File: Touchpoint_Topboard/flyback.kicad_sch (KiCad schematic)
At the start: 18 parts, among them Q1 NMOS, T1 DA2033-AL, U1 LT3750AEMS-TRPBF

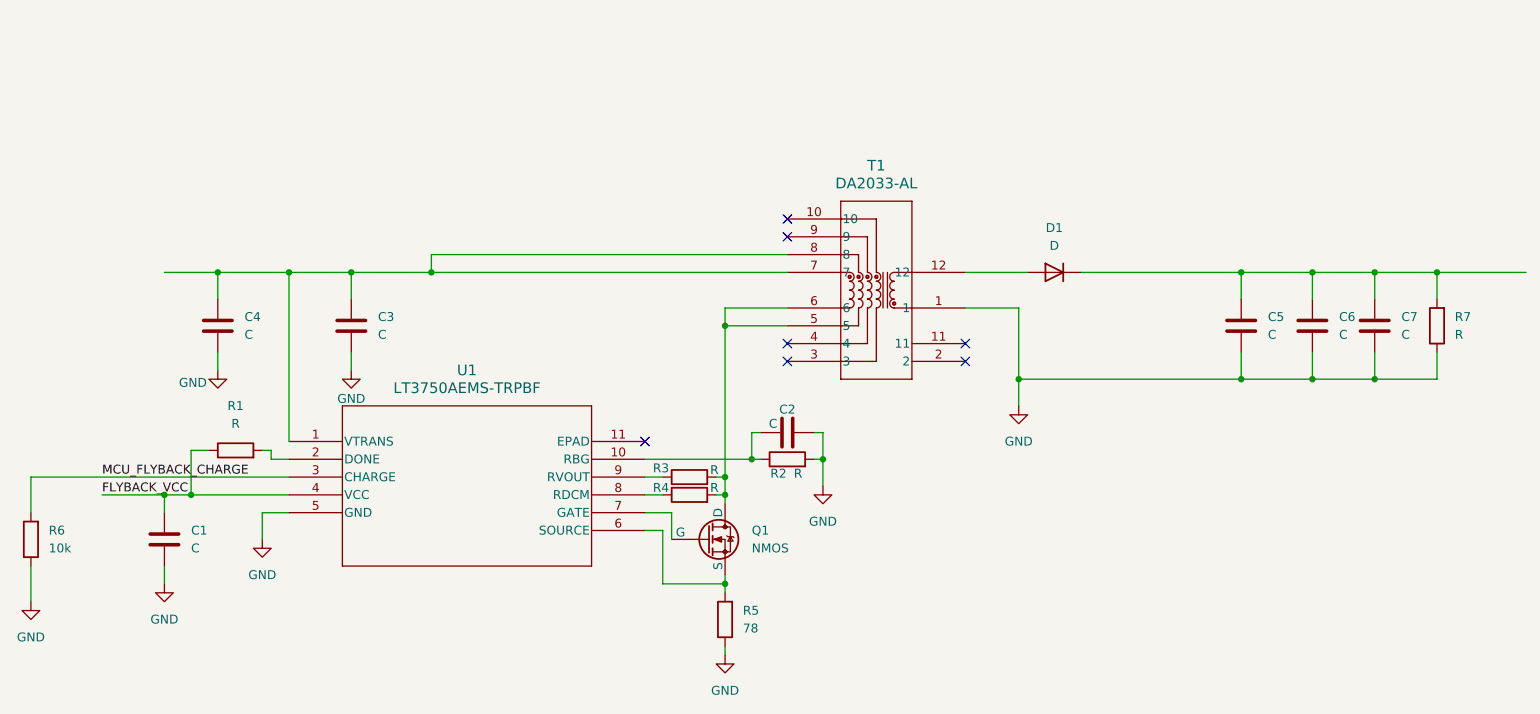
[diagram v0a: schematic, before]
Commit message: Finished assigning most footprints
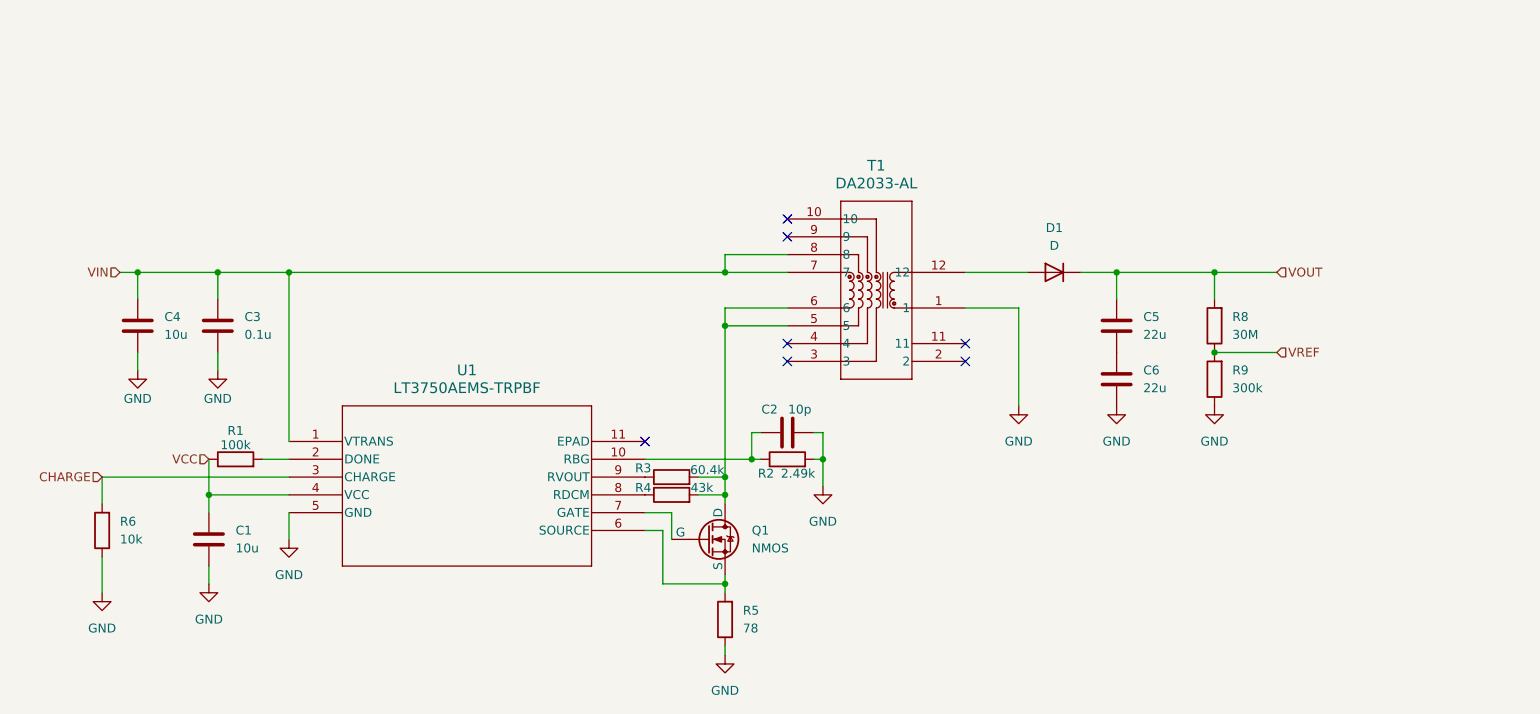
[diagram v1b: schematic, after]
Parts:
- removed C7: C, symbol Device:C
- removed R7: R, symbol Device:R
- added R8: 30M, Resistor_SMD:R_0402_1005Metric, symbol Device:R
- added R9: 300k, Resistor_SMD:R_0402_1005Metric, symbol Device:R
- C1, C4: value C -> 10u; footprint (none) -> Capacitor_SMD:C_0805_2012Metric
- C2: value C -> 10p; footprint (none) -> Capacitor_SMD:C_0402_1005Metric
- C3: value C -> 0.1u; footprint (none) -> Capacitor_SMD:C_0402_1005Metric
- C5, C6: value C -> 22u; footprint (none) -> Capacitor_SMD:C_0805_2012Metric
- D1: footprint (none) -> Touchpoint:SMB_DIO
- Q1: footprint (none) -> Touchpoint:SOT-89_3MC_MCH
- R1: value R -> 100k; footprint (none) -> Resistor_SMD:R_0402_1005Metric
- R2: value R -> 2.49k; footprint (none) -> Resistor_SMD:R_0402_1005Metric
- R3: value R -> 60.4k; footprint (none) -> Resistor_SMD:R_0402_1005Metric
- R4: value R -> 43k; footprint (none) -> Resistor_SMD:R_0402_1005Metric
- R5, R6: footprint (none) -> Resistor_SMD:R_0402_1005Metric
- T1: footprint DA2033-AL_COC -> Touchpoint:DA2032-AL
- U1: footprint MSOP10_05-08-1664_ADI -> Touchpoint:MSOP10_05-08-1664_ADI
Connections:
- net GND: now also C2.1, R9.1; no longer C2.2, C5.2
- net VOUT: now reaches C5.1, D1.1 (K)
- net VOUT: now also R8.2; no longer C6.1
- net VIN: now reaches C3.1, C4.1, T1.7, T1.8, U1.1 (VTRANS)
- net at R2.1, U1.10 (RBG): now also C2.2; no longer C2.1
- net FLYBACK_VCC renamed VCC
- net MCU_FLYBACK_CHARGE renamed CHARGE
- new net: C5.2, C6.1
- new net VREF: R8.1, R9.2
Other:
- moved on the sheet: C1, C3, C4, C5, R1, R3, R4, R6

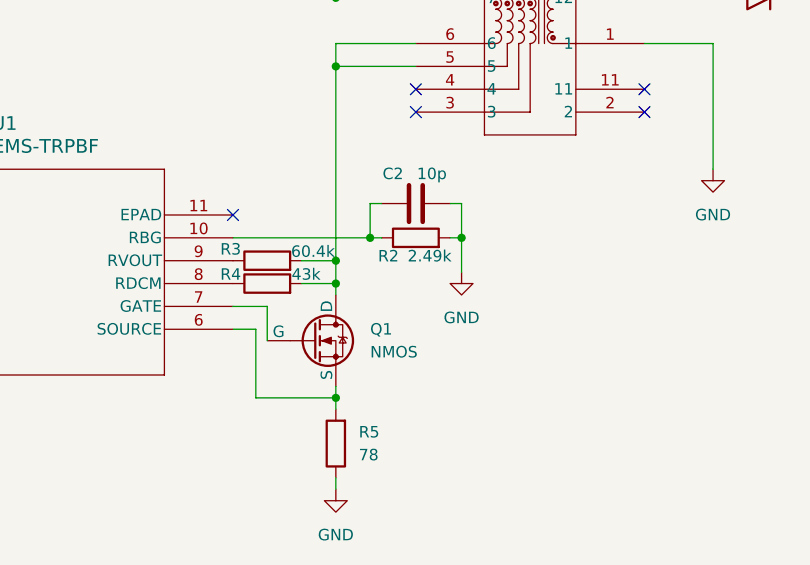
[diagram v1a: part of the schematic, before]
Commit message: Changed some component values based on availability
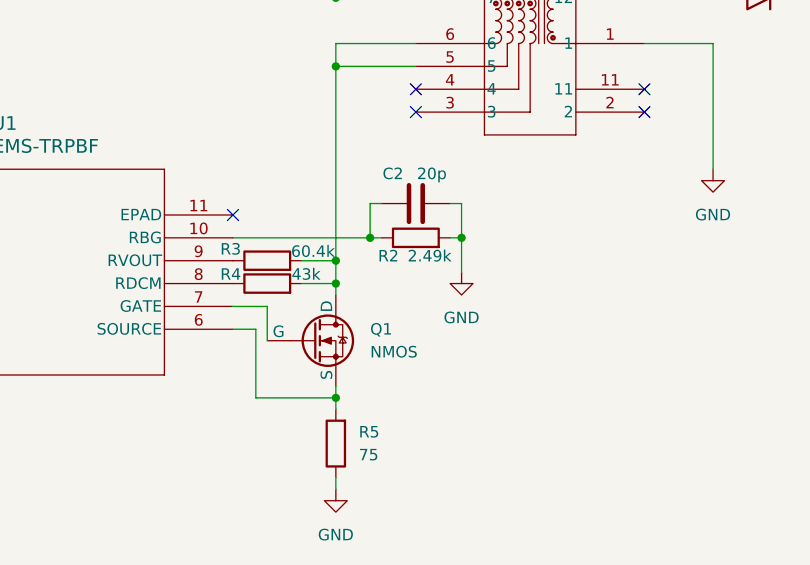
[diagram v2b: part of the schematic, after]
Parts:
- C2: value 10p -> 20p
- R5: value 78 -> 75
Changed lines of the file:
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@@
 			)
 		)
-		(property "Value" "78"
+		(property "Value" "75"
 			(at 171.45 118.1099 0)
 			(effects
@@
 			)
 		)
-		(property "Value" "10p"
+		(property "Value" "20p"
 			(at 179.578 86.868 90)
 			(effects

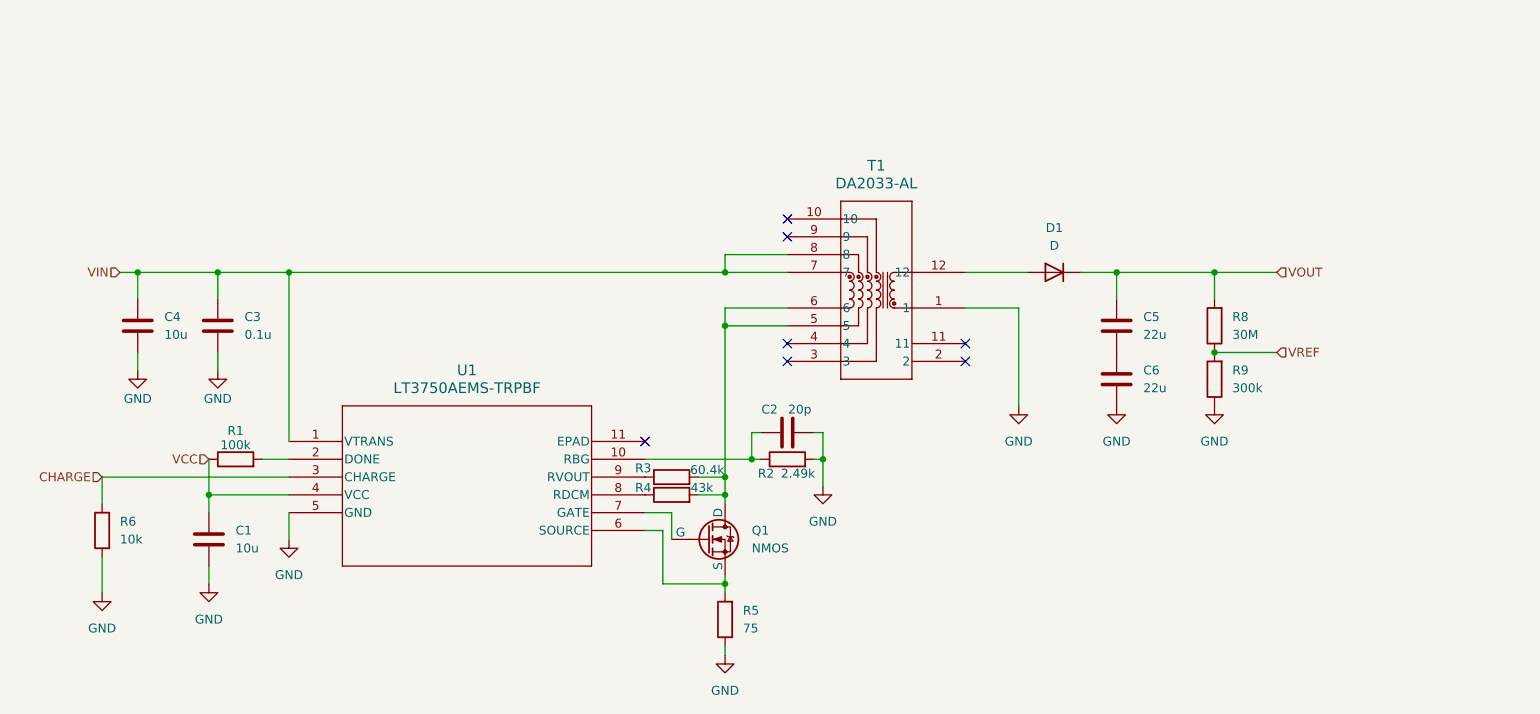
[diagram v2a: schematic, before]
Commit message: Finished assigning footprints and 3d models for both boards
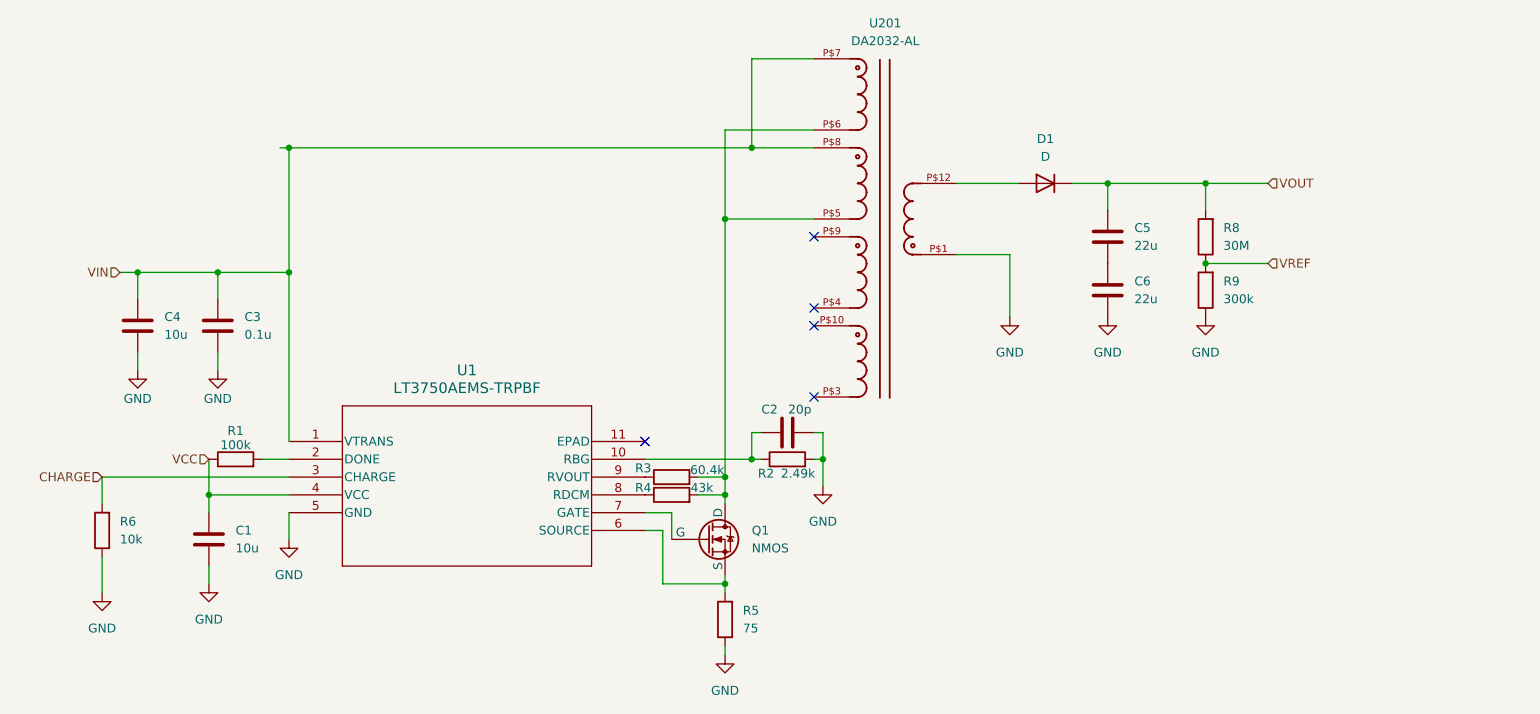
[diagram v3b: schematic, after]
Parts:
- removed T1: DA2033-AL, Touchpoint:DA2032-AL, symbol DL2032:DA2033-AL
- added U201: DA2032-AL, Touchpoint:DA2032-AL, symbol DA2032-AL:DA2032-AL
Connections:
- net GND: now also U201.P$1
- net VIN: now also U201.P$7, U201.P$8
- net at Q1.1 (D), R3.2, R4.2: now also U201.P$5, U201.P$6
- net at D1.2 (A): now also U201.P$12
- no-connect marks 7 -> 5
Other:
- moved on the sheet: C5, C6, D1, R8, R9

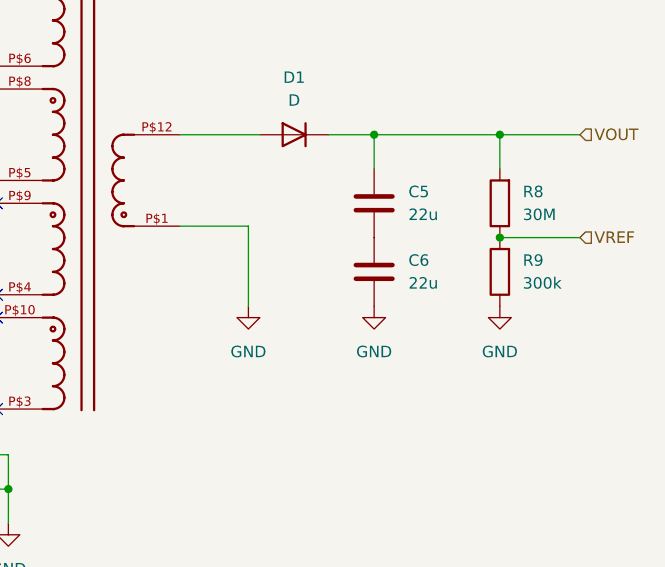
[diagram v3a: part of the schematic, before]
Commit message: Actually finished assigning footprints in 3d models
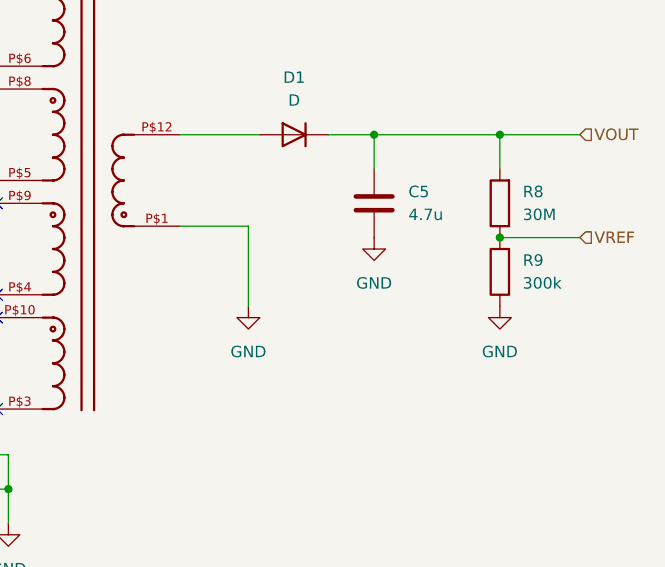
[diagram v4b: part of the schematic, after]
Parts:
- removed C6: 22u, Capacitor_SMD:C_0805_2012Metric, symbol Device:C
- C5: value 22u -> 4.7u; footprint Capacitor_SMD:C_0805_2012Metric -> Capacitor_THT:CP_Radial_D8.0mm_P3.50mm
- U1: footprint Touchpoint:MSOP10_05-08-1664_ADI -> Package_SO:MSOP-10-1EP_3x3mm_P0.5mm_EP1.68x1.88mm
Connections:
- net GND: now also C5.2
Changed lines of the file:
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@@
 	(symbol
 		(lib_id "power:GND")
-		(at 223.52 73.66 0)
+		(at 223.52 66.04 0)
 		(unit 1)
 		(exclude_from_sim no)
@@
 		(fields_autoplaced yes)
 		(property "Reference" "#PWR016"
-			(at 223.52 80.01 0)
+			(at 223.52 72.39 0)
 			(effects
 				(font
@@
 		)
 		(property "Value" "GND"
-			(at 223.52 78.74 0)
+			(at 223.52 71.12 0)
 			(effects
 				(font
@@
 		)
 		(property "Footprint" ""
-			(at 223.52 73.66 0)
+			(at 223.52 66.04 0)
 			(effects
 				(font
@@
 		)
 		(property "Datasheet" ""
-			(at 223.52 73.66 0)
+			(at 223.52 66.04 0)
 			(effects
 				(font
@@
 		)
 		(property "Description" "Power symbol creates a global label with name \"GND\" , ground"
-			(at 223.52 73.66 0)
+			(at 223.52 66.04 0)
 			(effects
 				(font
@@
 			)
 		)
-		(property "Footprint" "Touchpoint:MSOP10_05-08-1664_ADI"
+		(property "Footprint" "Package_SO:MSOP-10-1EP_3x3mm_P0.5mm_EP1.68x1.88mm"
 			(at 106.68 91.44 0)
 			(effects
@@
 	)
 	(symbol
-		(lib_id "Device:C")
-		(at 223.52 69.85 0)
-		(unit 1)
-		(exclude_from_sim no)
-		(in_bom yes)
-		(on_board yes)
-		(dnp no)
-		(fields_autoplaced yes)
-		(property "Reference" "C6"
-			(at 227.33 68.5799 0)
-			(effects
-				(font
-					(size 1.27 1.27)
-				)
-				(justify left)
-			)
-		)
-		(property "Value" "22u"
-			(at 227.33 71.1199 0)
-			(effects
-				(font
-					(size 1.27 1.27)
-				)
-				(justify left)
-			)
-		)
-		(property "Footprint" "Capacitor_SMD:C_0805_2012Metric"
-			(at 224.4852 73.66 0)
-			(effects
-				(font
-					(size 1.27 1.27)
-				)
-				(hide yes)
-			)
-		)
-		(property "Datasheet" "~"
-			(at 223.52 69.85 0)
-			(effects
-				(font
-					(size 1.27 1.27)
-				)
-				(hide yes)
-			)
-		)
-		(property "Description" "Unpolarized capacitor"
-			(at 223.52 69.85 0)
-			(effects
-				(font
-					(size 1.27 1.27)
-				)
-				(hide yes)
-			)
-		)
-		(pin "2"
-		)
-		(pin "1"
-		)
-		(instances
-			(project "Touchpoint_Topboard"
-				(path "/7efcba5d-f3d7-4197-a753-e42cd4117b88/41bd7ce1-1ba2-4b86-912b-61f5e6f9ab0c"
-					(reference "C6")
-					(unit 1)
-				)
-			)
-		)
-	)
-	(symbol
 		(lib_id "power:GND")
 		(at 237.49 73.66 0)
@@
 			)
 		)
-		(property "Value" "22u"
+		(property "Value" "4.7u"
 			(at 227.33 63.4999 0)
 			(effects
@@
 			)
 		)
-		(property "Footprint" "Capacitor_SMD:C_0805_2012Metric"
+		(property "Footprint" "Capacitor_THT:CP_Radial_D8.0mm_P3.50mm"
 			(at 224.4852 66.04 0)
 			(effects

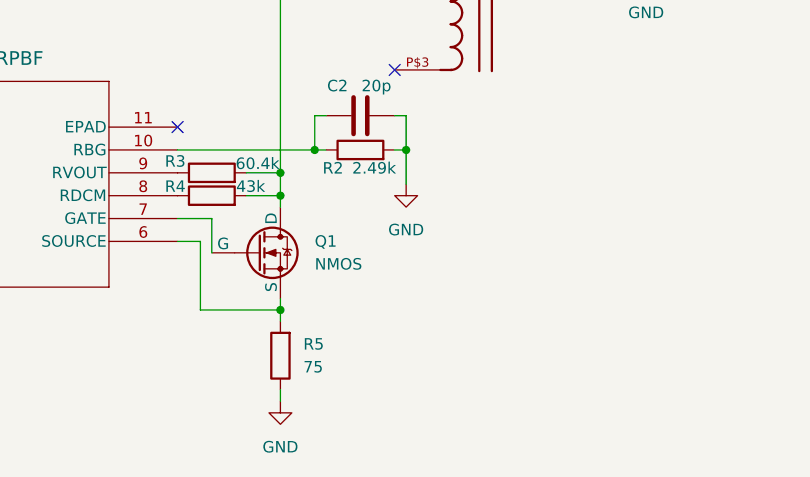
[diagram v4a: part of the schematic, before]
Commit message: Added minor final changes to schematic
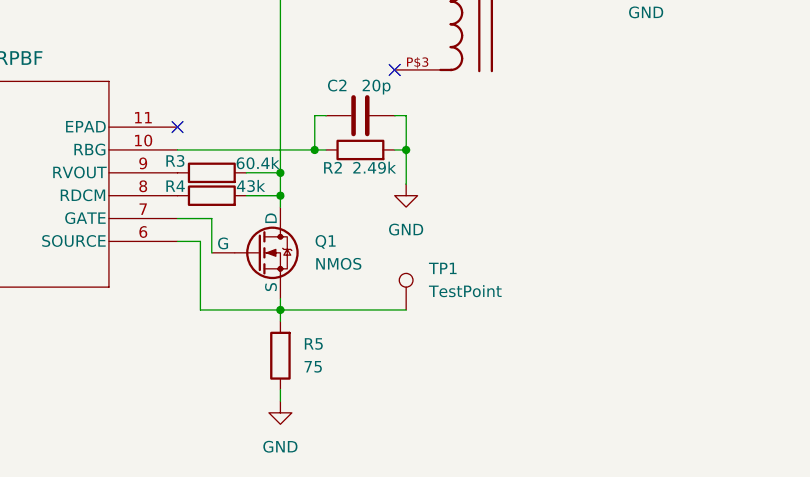
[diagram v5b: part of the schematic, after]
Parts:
- added TP1: TestPoint, TestPoint:TestPoint_Keystone_5019_Miniature, symbol Connector:TestPoint
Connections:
- net at Q1.3 (S), R5.2, U1.6 (SOURCE): now also TP1.1
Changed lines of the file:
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@@
+	(wire
+		(pts
+			(xy 168.91 111.76) (xy 182.88 111.76)
+		)
+		(stroke
+			(width 0)
+			(type default)
+		)
+	)
 	(wire
 		(pts
@@
 					(unit 1)
 				)
+			)
+		)
+	)
+	(symbol
+		(lib_id "Connector:TestPoint")
+		(at 182.88 111.76 0)
+		(unit 1)
+		(exclude_from_sim no)
+		(in_bom yes)
+		(on_board yes)
+		(dnp no)
+		(fields_autoplaced yes)
+		(property "Reference" "TP1"
+			(at 185.42 107.1879 0)
+			(effects
+				(font
+					(size 1.27 1.27)
+				)
+				(justify left)
+			)
+		)
+		(property "Value" "TestPoint"
+			(at 185.42 109.7279 0)
+			(effects
+				(font
+					(size 1.27 1.27)
+				)
+				(justify left)
+			)
+		)
+		(property "Footprint" "TestPoint:TestPoint_Keystone_5019_Miniature"
+			(at 187.96 111.76 0)
+			(effects
+				(font
+					(size 1.27 1.27)
+				)
+				(hide yes)
+			)
+		)
+		(property "Datasheet" "~"
+			(at 187.96 111.76 0)
+			(effects
+				(font
+					(size 1.27 1.27)
+				)
+				(hide yes)
+			)
+		)
+		(property "Description" "test point"
+			(at 182.88 111.76 0)
+			(effects
+				(font
+					(size 1.27 1.27)
+				)
+				(hide yes)
+			)
+		)
+		(pin "1"
+		)
+		(instances
+			(project ""
+				(path "/7efcba5d-f3d7-4197-a753-e42cd4117b88/41bd7ce1-1ba2-4b86-912b-61f5e6f9ab0c"
+					(reference "TP1")
+					(unit 1)
+				)
